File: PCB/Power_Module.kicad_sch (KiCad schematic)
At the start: 35 parts, among them Q1 AO3401A, Q2 LBSS84LT1G, Q3 LBSS84LT1G, U1 TP4056, U2 XC6206P, U3 OP07

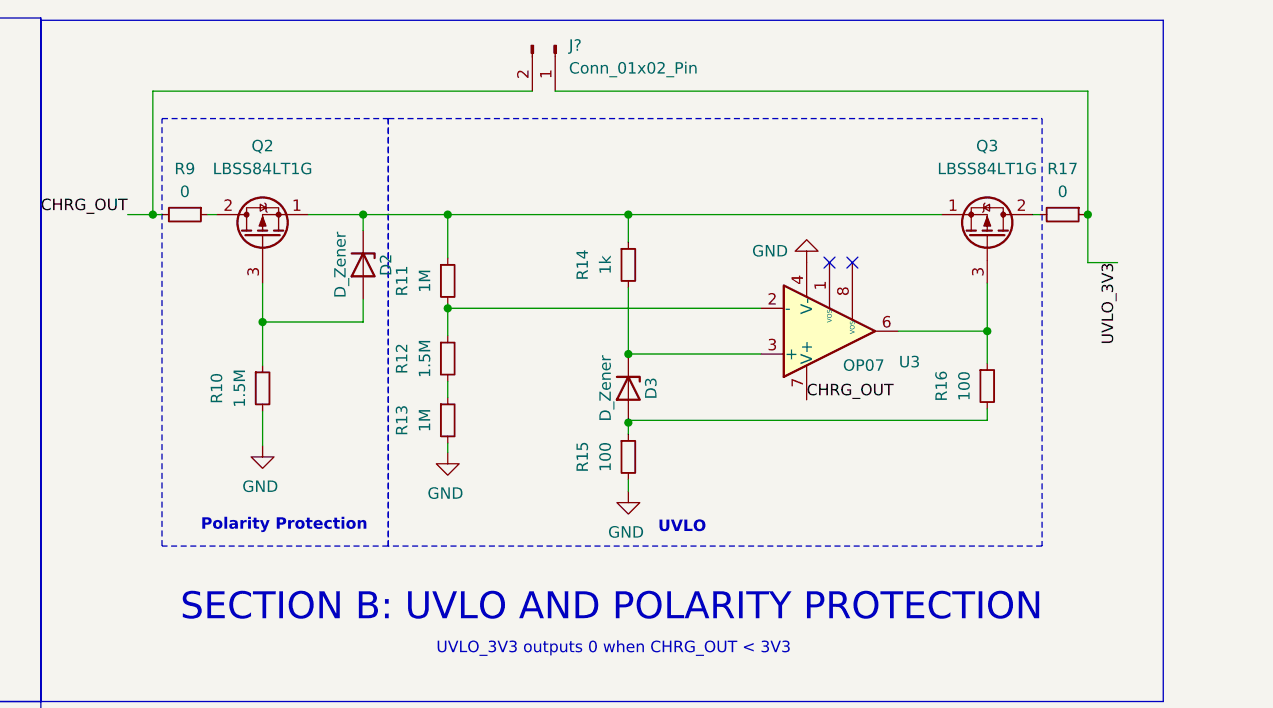
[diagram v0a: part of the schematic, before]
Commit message: updated power cct and PCB
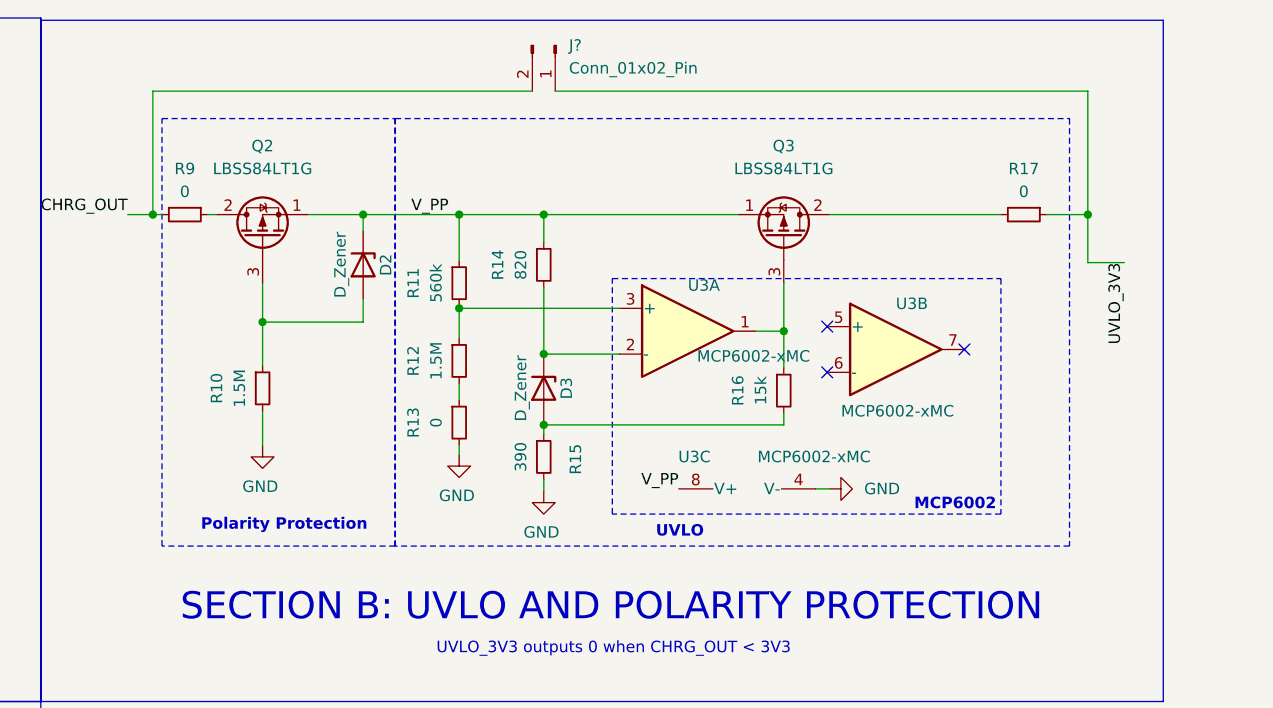
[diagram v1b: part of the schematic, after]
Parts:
- removed U3: OP07, JLC_Opamp:SOIC-8_L4.9-W3.9-P1.27-LS6.0-BL, symbol Amplifier_Operational:OP07
- added U3: MCP6002-xMC, Package_DFN_QFN:DFN-8-1EP_3x2mm_P0.5mm_EP1.75x1.45mm, symbol Amplifier_Operational:MCP6002-xMC
- R11: value 1M -> 560k; footprint Resistor_SMD:R_0805_2012Metric -> Resistor_SMD:R_0603_1608Metric
- R12: footprint Resistor_SMD:R_0805_2012Metric -> Resistor_SMD:R_0603_1608Metric
- R13: value 1M -> 0
- R14: value 1k -> 820
- R15: value 100 -> 390
- R16: value 100 -> 15k
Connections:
- net GND: now also U3.4 (V-), U3.9 (V-)
- net V_PP: now reaches D2.1 (K), Q2.1 (S), Q3.1 (S), R11.1, R14.1
- net V_PP: now also U3.8 (V+)
- net at R11.2, R12.1: now also U3.3 (+)
- net at D3.1 (K), R14.2: now also U3.2 (-)
- net at Q3.3 (G), R16.1: now also U3.1
- no-connect marks 2 -> 3
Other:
- note added: "MCP6002"
- moved on the sheet: D3, Q3, R11, R12, R13, R14, R15, R16, R17

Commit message: simon changes
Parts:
- added D4: D_Schottky, JLC_Diodes:SOD-323_L1.8-W1.3-LS2.5-RD, symbol Device:D_Schottky
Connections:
- net V_BAT+: now also D4.2 (A); no longer Q1.2 (S)
- new net: D4.1 (K), Q1.2 (S)
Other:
- moved on the sheet: R6, R8
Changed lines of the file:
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@@
   (junction (at 49.022 42.164) (diameter 0) (color 0 0 0 0)
   )
-  (junction (at 120.904 43.434) (diameter 0) (color 0 0 0 0)
+  (junction (at 111.506 43.434) (diameter 0) (color 0 0 0 0)
   )
   (junction (at 215.646 34.544) (diameter 0) (color 0 0 0 0)
@@
     (stroke (width 0) (type default))
   )
-  (wire (pts (xy 120.904 43.434) (xy 124.714 43.434))
-    (stroke (width 0) (type default))
-  )
   (wire (pts (xy 44.704 42.164) (xy 44.704 52.324))
     (stroke (width 0) (type default))
@@
     (stroke (width 0) (type default))
   )
-  (wire (pts (xy 118.364 43.434) (xy 120.904 43.434))
-    (stroke (width 0) (type default))
-  )
   (wire (pts (xy 215.646 37.592) (xy 215.646 34.544))
     (stroke (width 0) (type default))
@@
     (stroke (width 0) (type default))
   )
+  (wire (pts (xy 121.92 43.434) (xy 124.714 43.434))
+    (stroke (width 0) (type default))
+  )
   (wire (pts (xy 276.098 39.878) (xy 280.162 39.878))
     (stroke (width 0) (type default))
@@
     (stroke (width 0) (type default))
   )
-  (wire (pts (xy 109.474 32.004) (xy 109.474 45.974))
+  (wire (pts (xy 109.474 32.004) (xy 109.474 33.02))
     (stroke (width 0) (type default))
   )
@@
     (stroke (width 0) (type default))
   )
+  (wire (pts (xy 109.22 43.434) (xy 111.506 43.434))
+    (stroke (width 0) (type default))
+  )
   (wire (pts (xy 118.11 120.142) (xy 118.11 115.824))
     (stroke (width 0) (type default))
@@
     (stroke (width 0) (type default))
   )
-  (wire (pts (xy 120.904 47.244) (xy 120.904 43.434))
+  (wire (pts (xy 111.506 47.244) (xy 111.506 43.434))
     (stroke (width 0) (type default))
   )
@@
     (stroke (width 0) (type default))
   )
+  (wire (pts (xy 111.506 43.434) (xy 114.3 43.434))
+    (stroke (width 0) (type default))
+  )
   (wire (pts (xy 184.404 56.388) (xy 184.404 60.198))
     (stroke (width 0) (type default))
@@
     (stroke (width 0) (type default))
   )
-  (wire (pts (xy 101.219 43.434) (xy 113.284 43.434))
+  (wire (pts (xy 101.219 43.434) (xy 104.14 43.434))
     (stroke (width 0) (type default))
   )
@@
     (effects (font (size 1.27 1.27)) (justify left))
   )
-  (hierarchical_label "V_BAT+" (shape output) (at 120.904 47.244 270) (fields_autoplaced)
+  (hierarchical_label "V_BAT+" (shape output) (at 111.506 47.244 270) (fields_autoplaced)
     (effects (font (size 1.27 1.27)) (justify right))
   )
@@
     )
   )
-  (symbol (lib_id "Device:R_Small") (at 115.824 43.434 270) (unit 1)
-    (in_bom yes) (on_board yes) (dnp no)
-    (property "Reference" "R8" (at 115.824 38.354 90)
-      (effects (font (size 1.27 1.27)))
-    )
-    (property "Value" "0" (at 115.824 40.894 90)
-      (effects (font (size 1.27 1.27)))
-    )
-    (property "Footprint" "Resistor_SMD:R_0805_2012Metric" (at 115.824 43.434 0)
-      (effects (font (size 1.27 1.27)) hide)
-    )
-    (property "Datasheet" "~" (at 115.824 43.434 0)
+  (symbol (lib_id "Device:R_Small") (at 106.68 43.434 270) (unit 1)
+    (in_bom yes) (on_board yes) (dnp no)
+    (property "Reference" "R8" (at 106.934 45.974 90)
+      (effects (font (size 1.27 1.27)))
+    )
+    (property "Value" "0" (at 106.934 48.514 90)
+      (effects (font (size 1.27 1.27)))
+    )
+    (property "Footprint" "Resistor_SMD:R_0805_2012Metric" (at 106.68 43.434 0)
+      (effects (font (size 1.27 1.27)) hide)
+    )
+    (property "Datasheet" "~" (at 106.68 43.434 0)
       (effects (font (size 1.27 1.27)) hide)
     )
@@
         (path "/e63e39d7-6ac0-4ffd-8aa3-1841a4541b55"
           (reference "#PWR?") (unit 1)
+        )
+      )
+    )
+  )
+  (symbol (lib_id "Device:D_Schottky") (at 118.11 43.434 180) (unit 1)
+    (in_bom yes) (on_board yes) (dnp no) (fields_autoplaced)
+    (property "Reference" "D4" (at 118.4275 38.1 0)
+      (effects (font (size 1.27 1.27)))
+    )
+    (property "Value" "D_Schottky" (at 118.4275 40.64 0)
+      (effects (font (size 1.27 1.27)))
+    )
+    (property "Footprint" "JLC_Diodes:SOD-323_L1.8-W1.3-LS2.5-RD" (at 118.11 43.434 0)
+      (effects (font (size 1.27 1.27)) hide)
+    )
+    (property "Datasheet" "~" (at 118.11 43.434 0)
+      (effects (font (size 1.27 1.27)) hide)
+    )
+    (pin "1")
+    (pin "2")
+    (instances
+      (project "HAT"
+        (path "/40f36b19-a08c-43e7-88a6-ec8387939712/13666b47-888a-4bed-b522-fee751a1c440"
+          (reference "D4") (unit 1)
+        )
+      )
+      (project "Power_Module"
+        (path "/9518a89f-42c8-4f0b-818e-9ddc6754f3b2"
+          (reference "D?") (unit 1)
         )
       )
@@
     )
   )
-  (symbol (lib_id "power:GND") (at 109.474 51.054 0) (unit 1)
-    (in_bom yes) (on_board yes) (dnp no) (fields_autoplaced)
-    (property "Reference" "#PWR010" (at 109.474 57.404 0)
-      (effects (font (size 1.27 1.27)) hide)
-    )
-    (property "Value" "GND" (at 109.474 55.499 0)
-      (effects (font (size 1.27 1.27)))
-    )
-    (property "Footprint" "" (at 109.474 51.054 0)
-      (effects (font (size 1.27 1.27)) hide)
-    )
-    (property "Datasheet" "" (at 109.474 51.054 0)
+  (symbol (lib_id "power:GND") (at 109.474 38.1 0) (unit 1)
+    (in_bom yes) (on_board yes) (dnp no)
+    (property "Reference" "#PWR010" (at 109.474 44.45 0)
+      (effects (font (size 1.27 1.27)) hide)
+    )
+    (property "Value" "GND" (at 106.172 38.354 0)
+      (effects (font (size 1.27 1.27)))
+    )
+    (property "Footprint" "" (at 109.474 38.1 0)
+      (effects (font (size 1.27 1.27)) hide)
+    )
+    (property "Datasheet" "" (at 109.474 38.1 0)
       (effects (font (size 1.27 1.27)) hide)
     )
@@
     )
   )
-  (symbol (lib_id "Device:R_Small") (at 109.474 48.514 180) (unit 1)
-    (in_bom yes) (on_board yes) (dnp no)
-    (property "Reference" "R6" (at 113.2332 50.9524 0)
-      (effects (font (size 1.27 1.27)))
-    )
-    (property "Value" "10k" (at 113.2332 48.4124 0)
-      (effects (font (size 1.27 1.27)))
-    )
-    (property "Footprint" "Resistor_SMD:R_0805_2012Metric" (at 109.474 48.514 0)
-      (effects (font (size 1.27 1.27)) hide)
-    )
-    (property "Datasheet" "~" (at 109.474 48.514 0)
-      (effects (font (size 1.27 1.27)) hide)
-    )
+  (symbol (lib_id "Device:R_Small") (at 109.474 35.56 180) (unit 1)
+    (in_bom yes) (on_board yes) (dnp no)
+    (property "Reference" "R6" (at 113.2332 37.9984 0)
+      (effects (font (size 1.27 1.27)))
+    )
+    (property "Value" "10k" (at 113.2332 35.4584 0)
+      (effects (font (size 1.27 1.27)))
+    )
+    (property "Footprint" "Resistor_SMD:R_0805_2012Metric" (at 109.474 35.56 0)
+      (effects (font (size 1.27 1.27)) hide)
+    )
+    (property "Datasheet" "~" (at 109.474 35.56 0)
+      (effects (font (size 1.27 1.27)) hide)
+    )

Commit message: final pcb and chematic changes
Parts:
- added D5: D_Schottky, JLC_Diodes:SOD-323_L1.8-W1.3-LS2.5-RD, symbol Device:D_Schottky
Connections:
- net at C1.2, D1.2 (A), LED1.2 (A)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: now also D5.1 (K); no longer R2.2
- new net: D5.2 (A), R2.2
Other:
- moved on the sheet: R2
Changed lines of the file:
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@@
   (junction (at 118.11 115.824) (diameter 0) (color 0 0 0 0)
   )
+  (junction (at 48.514 42.164) (diameter 0) (color 0 0 0 0)
+  )
   (junction (at 56.007 120.142) (diameter 0) (color 0 0 0 0)
-  )
-  (junction (at 49.022 42.164) (diameter 0) (color 0 0 0 0)
   )
   (junction (at 111.506 43.434) (diameter 0) (color 0 0 0 0)
@@
   (no_connect (at 262.382 49.53))
   (no_connect (at 247.142 52.07))
+  (wire (pts (xy 48.514 42.164) (xy 54.229 42.164))
+    (stroke (width 0) (type default))
+  )
   (wire (pts (xy 101.219 49.784) (xy 101.219 51.689))
     (stroke (width 0) (type default))
@@
     (stroke (width 0) (type default))
   )
-  (wire (pts (xy 49.022 42.164) (xy 54.229 42.164))
-    (stroke (width 0) (type default))
-  )
   (wire (pts (xy 239.268 47.498) (xy 242.316 47.498))
     (stroke (width 0) (type default))
@@
     (stroke (width 0) (type default))
   )
-  (wire (pts (xy 44.704 42.164) (xy 49.022 42.164))
+  (wire (pts (xy 44.704 42.164) (xy 48.514 42.164))
     (stroke (width 0) (type default))
   )
@@
     (stroke (width 0) (type default))
   )
-  (wire (pts (xy 48.514 26.416) (xy 48.514 27.051))
-    (stroke (width 0) (type default))
-  )
   (wire (pts (xy 245.872 65.024) (xy 247.396 65.024))
     (stroke (width 0) (type default))
@@
     (stroke (width 0) (type default))
   )
-  (wire (pts (xy 49.022 36.322) (xy 49.022 42.164))
+  (wire (pts (xy 48.514 31.496) (xy 48.514 32.766))
     (stroke (width 0) (type default))
   )
@@
     (stroke (width 0) (type default))
   )
-  (wire (pts (xy 49.022 27.051) (xy 49.022 31.242))
+  (wire (pts (xy 48.514 19.812) (xy 48.514 26.416))
     (stroke (width 0) (type default))
   )
@@
     (stroke (width 0) (type default))
   )
-  (wire (pts (xy 48.514 27.051) (xy 49.022 27.051))
-    (stroke (width 0) (type default))
-  )
   (wire (pts (xy 111.506 43.434) (xy 114.3 43.434))
     (stroke (width 0) (type default))
@@
   )
   (wire (pts (xy 206.248 44.958) (xy 206.248 48.26))
+    (stroke (width 0) (type default))
+  )
+  (wire (pts (xy 48.514 40.386) (xy 48.514 42.164))
     (stroke (width 0) (type default))
   )
@@
     (effects (font (size 1.27 1.27)) (justify left bottom))
   )
-  (hierarchical_label "USB_IN_5V" (shape input) (at 48.514 26.416 180) (fields_autoplaced)
+  (hierarchical_label "USB_IN_5V" (shape input) (at 48.514 19.812 180) (fields_autoplaced)
     (effects (font (size 1.27 1.27)) (justify right))
   )
@@
     )
   )
-  (symbol (lib_id "Device:R_Small") (at 49.022 33.782 0) (unit 1)
-    (in_bom yes) (on_board yes) (dnp no)
-    (property "Reference" "R2" (at 43.942 33.782 0)
-      (effects (font (size 1.27 1.27)))
-    )
-    (property "Value" "0" (at 46.482 33.782 0)
-      (effects (font (size 1.27 1.27)))
-    )
-    (property "Footprint" "Resistor_SMD:R_0805_2012Metric" (at 49.022 33.782 0)
-      (effects (font (size 1.27 1.27)) hide)
-    )
-    (property "Datasheet" "~" (at 49.022 33.782 0)
+  (symbol (lib_id "Device:R_Small") (at 48.514 28.956 0) (unit 1)
+    (in_bom yes) (on_board yes) (dnp no)
+    (property "Reference" "R2" (at 43.434 28.956 0)
+      (effects (font (size 1.27 1.27)))
+    )
+    (property "Value" "0" (at 45.974 28.956 0)
+      (effects (font (size 1.27 1.27)))
+    )
+    (property "Footprint" "Resistor_SMD:R_0805_2012Metric" (at 48.514 28.956 0)
+      (effects (font (size 1.27 1.27)) hide)
+    )
+    (property "Datasheet" "~" (at 48.514 28.956 0)
       (effects (font (size 1.27 1.27)) hide)
     )
@@
         )
       )
+    )
+  )
+  (symbol (lib_id "Device:D_Schottky") (at 48.514 36.576 90) (unit 1)
+    (in_bom yes) (on_board yes) (dnp no) (fields_autoplaced)
+    (property "Reference" "D5" (at 53.848 36.8935 0)
+      (effects (font (size 1.27 1.27)))
+    )
+    (property "Value" "D_Schottky" (at 51.308 36.8935 0)
+      (effects (font (size 1.27 1.27)))
+    )
+    (property "Footprint" "JLC_Diodes:SOD-323_L1.8-W1.3-LS2.5-RD" (at 48.514 36.576 0)
+      (effects (font (size 1.27 1.27)) hide)
+    )
+    (property "Datasheet" "~" (at 48.514 36.576 0)
+      (effects (font (size 1.27 1.27)) hide)
+    )
+    (pin "1")
+    (pin "2")
+    (instances
+      (project "HAT"
+        (path "/40f36b19-a08c-43e7-88a6-ec8387939712/13666b47-888a-4bed-b522-fee751a1c440"
+          (reference "D5") (unit 1)
+        )
+      )
+      (project "Power_Module"
+        (path "/9518a89f-42c8-4f0b-818e-9ddc6754f3b2"
+          (reference "D?") (unit 1)
+        )
+      )

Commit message: actual final pcb and schematic changes
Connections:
- net at C1.2, D5.1 (K), LED1.2 (A)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: no longer D1.2 (A), Q1.1 (G), R6.2
- net at D5.2 (A), R2.2: now also D1.2 (A), Q1.1 (G), R6.2
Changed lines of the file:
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@@
   (junction (at 96.012 120.142) (diameter 0) (color 0 0 0 0)
   )
+  (junction (at 48.514 32.004) (diameter 0) (color 0 0 0 0)
+  )
   (junction (at 118.11 115.824) (diameter 0) (color 0 0 0 0)
   )
@@
   )
   (junction (at 206.248 44.958) (diameter 0) (color 0 0 0 0)
-  )
-  (junction (at 59.944 42.164) (diameter 0) (color 0 0 0 0)
   )
   (junction (at 101.219 43.434) (diameter 0) (color 0 0 0 0)
@@
     (stroke (width 0) (type default))
   )
-  (wire (pts (xy 59.944 32.004) (xy 109.474 32.004))
+  (wire (pts (xy 48.514 32.004) (xy 109.474 32.004))
     (stroke (width 0) (type default))
   )
@@
     (stroke (width 0) (type default))
   )
-  (wire (pts (xy 59.944 42.164) (xy 65.024 42.164))
-    (stroke (width 0) (type default))
-  )
   (wire (pts (xy 37.592 120.142) (xy 40.132 120.142))
     (stroke (width 0) (type default))
@@
     (stroke (width 0) (type default))
   )
-  (wire (pts (xy 59.944 42.164) (xy 59.944 32.004))
-    (stroke (width 0) (type default))
-  )
   (wire (pts (xy 44.704 42.164) (xy 48.514 42.164))
     (stroke (width 0) (type default))
@@
     (stroke (width 0) (type default))
   )
-  (wire (pts (xy 54.229 42.164) (xy 59.944 42.164))
+  (wire (pts (xy 54.229 42.164) (xy 65.024 42.164))
     (stroke (width 0) (type default))
   )
@@
     (stroke (width 0) (type default))
   )
-  (wire (pts (xy 48.514 31.496) (xy 48.514 32.766))
-    (stroke (width 0) (type default))
-  )
+  (wire (pts (xy 48.514 32.004) (xy 48.514 32.766))
+    (stroke (width 0) (type default))
+  )
+  (wire (pts (xy 48.514 31.496) (xy 48.514 32.004))
+    (stroke (width 0) (type default))
+  )
